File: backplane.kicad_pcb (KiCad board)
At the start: 4 copper layers, 110 x 90 mm, 45 parts, among them IC1 SiC437AED-T1-GE3, J1 46010-0622, J2 46010-0622, J4 212520-1006, J5 XT60PW-F

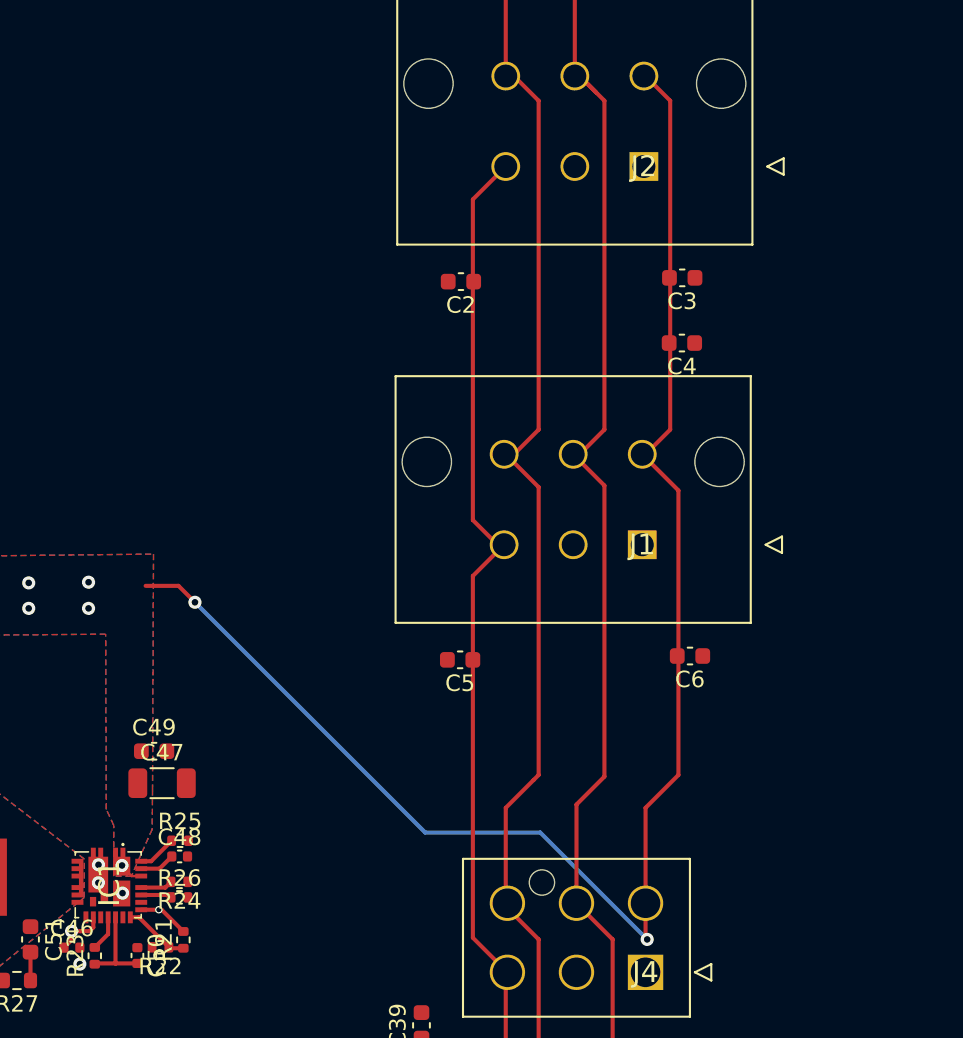
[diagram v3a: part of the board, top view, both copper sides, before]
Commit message: reducing more DRCs
zone violations etc
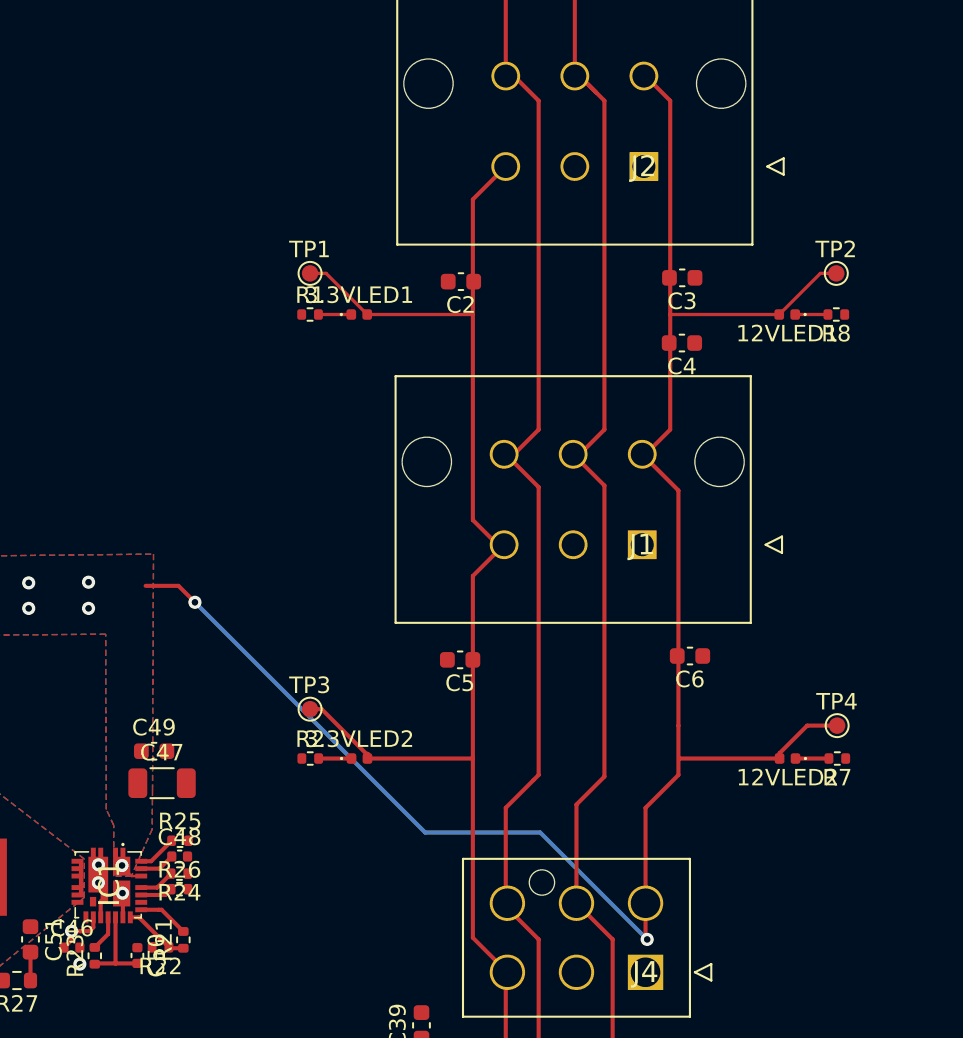
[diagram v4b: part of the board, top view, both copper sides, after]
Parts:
- added 12VLED1: 12VLED, LED_SMD:LED_0402_1005Metric, F.Cu at (160.0, 90.0)
- added 12VLED2: 12VLED, LED_SMD:LED_0402_1005Metric, F.Cu at (160.0, 117.0)
- added 3.3VLED1: 3.3VLED, LED_SMD:LED_0402_1005Metric, F.Cu at (134.0, 90.0)
- added 3.3VLED2: 3.3VLED, LED_SMD:LED_0402_1005Metric, F.Cu at (134.0, 117.0)
- added R1: 1k, Resistor_SMD:R_0402_1005Metric, F.Cu at (131.0, 90.0)
- added R2: 1k, Resistor_SMD:R_0402_1005Metric, F.Cu at (131.0, 117.0)
- added R7: 1k, Resistor_SMD:R_0402_1005Metric, F.Cu at (163.1, 117.0)
- added R8: 1k, Resistor_SMD:R_0402_1005Metric, F.Cu at (163.0, 90.0)
- added TP1: TestPoint, TestPoint:TestPoint_Pad_D1.0mm, F.Cu at (131.0, 87.5)
- added TP2: TestPoint, TestPoint:TestPoint_Pad_D1.0mm, F.Cu at (163.0, 87.5)
- added TP3: TestPoint, TestPoint:TestPoint_Pad_D1.0mm, F.Cu at (131.0, 114.0)
- added TP4: TestPoint, TestPoint:TestPoint_Pad_D1.0mm, F.Cu at (163.1, 115.0)
- moved R24 0.50 mm to (123.1, 124.0)
- moved R26 0.50 mm to (123.1, 124.9)
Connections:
- J5 pad 2: /GND -> GND
- J5 pad S1: /GND -> GND
- J5 pad S2: /GND -> GND
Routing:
- net +3.3V: track 57.4 -> 79.6 mm
- net +12V: track 95.5 -> 117.3 mm
- net GND: track 0.50 -> 3.26 mm
- net Net-(12VLED2-K): track 0.00 -> 2.03 mm
- net Net-(3.3VLED2-K): track 0.00 -> 2.00 mm
- net Net-(3.3VLED1-K): track 0.00 -> 2.00 mm
- net Net-(12VLED1-K): track 0.00 -> 1.99 mm
- net RBUS_uC_V: vias 1 -> 0
